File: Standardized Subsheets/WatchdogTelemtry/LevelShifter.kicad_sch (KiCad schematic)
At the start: 1 part, among them U6 LSF0204QPWRQ1

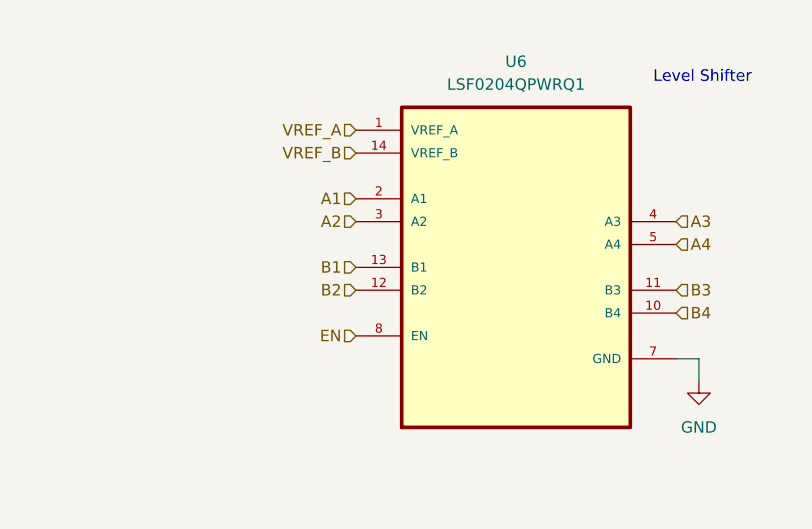
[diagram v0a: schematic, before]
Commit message: adding watchdog
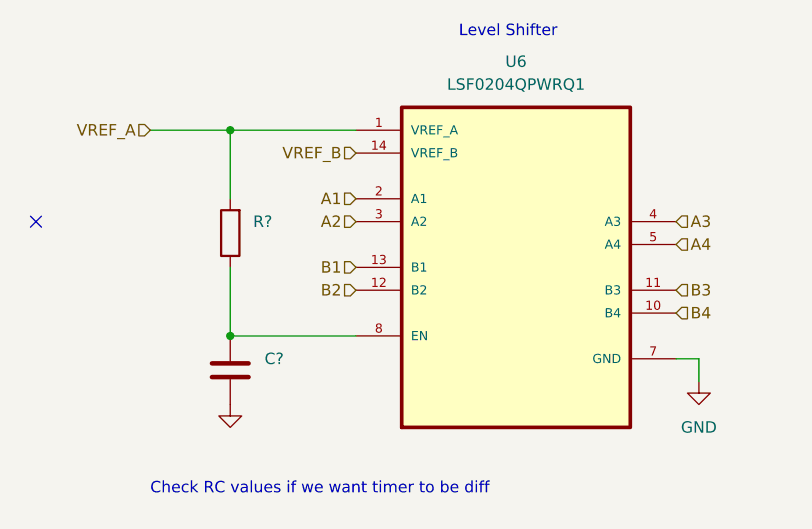
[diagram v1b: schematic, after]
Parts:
- added C?: (no value), symbol Device:C
- added R?: (no value), symbol Device:R
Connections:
- net GND: now also C?.2
- net VREF_A: now also R?.2
- net EN: no longer names the net of U6.8 (EN)
- net EN: now also C?.1, R?.1
- no-connect marks 0 -> 1
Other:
- note added: "Check RC values if we want timer to be diff"
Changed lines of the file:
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@@
 (kicad_sch (version 20211123) (generator eeschema)
   (paper "A4")
+  (junction (at 50.8 82.55) (diameter 0) (color 0 0 0 0)
+  )
+  (junction (at 50.8 59.69) (diameter 0) (color 0 0 0 0)
+  )
+  (no_connect (at 29.21 69.85))
+  (wire (pts (xy 50.8 59.69) (xy 50.8 67.31))
+    (stroke (width 0) (type default) (color 0 0 0 0))
+  )
+  (wire (pts (xy 41.91 59.69) (xy 50.8 59.69))
+    (stroke (width 0) (type default) (color 0 0 0 0))
+  )
+  (wire (pts (xy 50.8 59.69) (xy 64.77 59.69))
+    (stroke (width 0) (type default) (color 0 0 0 0))
+  )
+  (wire (pts (xy 50.8 74.93) (xy 50.8 82.55))
+    (stroke (width 0) (type default) (color 0 0 0 0))
+  )
+  (wire (pts (xy 50.8 82.55) (xy 64.77 82.55))
+    (stroke (width 0) (type default) (color 0 0 0 0))
+  )
   (wire (pts (xy 102.87 87.63) (xy 102.87 85.09))
     (stroke (width 0) (type default) (color 0 0 0 0))
@@
     (stroke (width 0) (type default) (color 0 0 0 0))
   )
-  (text "Level Shifter\n" (at 97.79 54.61 0)
+  (text "Check RC values if we want timer to be diff\n" (at 41.91 100.33 0)
     (effects (font (size 1.27 1.27)) (justify left bottom))
   )
-  (hierarchical_label "EN" (shape input) (at 64.77 82.55 180)
-    (effects (font (size 1.27 1.27)) (justify right))
+  (text "Level Shifter\n" (at 76.2 49.53 0)
+    (effects (font (size 1.27 1.27)) (justify left bottom))
   )
   (hierarchical_label "A3" (shape input) (at 100.33 69.85 0)
@@
     (effects (font (size 1.27 1.27)) (justify left))
   )
-  (hierarchical_label "VREF_A" (shape input) (at 64.77 59.69 180)
+  (hierarchical_label "VREF_A" (shape input) (at 41.91 59.69 180)
     (effects (font (size 1.27 1.27)) (justify right))
   )
   (hierarchical_label "A4" (shape input) (at 100.33 72.39 0)
     (effects (font (size 1.27 1.27)) (justify left))
+  )
+  (symbol (lib_id "Device:R") (at 50.8 71.12 180) (unit 1)
+    (in_bom yes) (on_board yes) (fields_autoplaced)
+    (property "Reference" "R?" (id 0) (at 53.34 69.8499 0)
+      (effects (font (size 1.27 1.27)) (justify right))
+    )
+    (property "Value" "" (id 1) (at 53.34 72.3899 0)
+      (effects (font (size 1.27 1.27)) (justify right))
+    )
+    (property "Footprint" "" (id 2) (at 52.578 71.12 90)
+      (effects (font (size 1.27 1.27)) hide)
+    )
+    (property "Datasheet" "~" (id 3) (at 50.8 71.12 0)
+      (effects (font (size 1.27 1.27)) hide)
+    )
+    (pin "1")
+    (pin "2")
+  )
+  (symbol (lib_id "Device:C") (at 50.8 86.36 0) (unit 1)
+    (in_bom yes) (on_board yes) (fields_autoplaced)
+    (property "Reference" "C?" (id 0) (at 54.61 85.0899 0)
+      (effects (font (size 1.27 1.27)) (justify left))
+    )
+    (property "Value" "" (id 1) (at 54.61 87.6299 0)
+      (effects (font (size 1.27 1.27)) (justify left))
+    )
+    (property "Footprint" "" (id 2) (at 51.7652 90.17 0)
+      (effects (font (size 1.27 1.27)) hide)
+    )
+    (property "Datasheet" "~" (id 3) (at 50.8 86.36 0)
+      (effects (font (size 1.27 1.27)) hide)
+    )
+    (pin "1")
+    (pin "2")
+  )
+  (symbol (lib_id "power:GND") (at 50.8 90.17 0) (unit 1)
+    (in_bom yes) (on_board yes) (fields_autoplaced)
+    (property "Reference" "#PWR?" (id 0) (at 50.8 96.52 0)
+      (effects (font (size 1.27 1.27)) hide)
+    )
+    (property "Value" "" (id 1) (at 50.8 95.25 0))
+    (property "Footprint" "" (id 2) (at 50.8 90.17 0)
+      (effects (font (size 1.27 1.27)) hide)
+    )
+    (property "Datasheet" "" (id 3) (at 50.8 90.17 0)
+      (effects (font (size 1.27 1.27)) hide)
+    )
+    (pin "1")
   )
   (symbol (lib_id "LSF0204QPWRQ1:LSF0204QPWRQ1") (at 82.55 74.93 0) (unit 1)
@@
       (effects (font (size 1.27 1.27)) (justify left bottom) hide)
     )
-    (property "Datasheet" "" (id 3) (at 82.55 74.93 0)
+    (property "Datasheet" "https://www.ti.com/lit/ds/symlink/lsf0204-q1.pdf?ts=1668512599421&ref_url=https%253A%252F%252Fwww.ti.com%252Fproduct%252FLSF0204-Q1%252Fpart-details%252FLSF0204QPWRQ1%253Futm_source%253Dgoogle%2526utm_medium%253Dcpc%2526utm_campaign%253Docb-tistore-promo-asc_opn_en-cpc-storeic-google-wwe%2526utm_content%253DDevice%2526ds_k%253DLSF0204QPWRQ1%2526DCM%253Dyes%2526gclid%253DCjwKCAiAjs2bBhACEiwALTBWZYsrvH2Lh7WvnQkqr_CpO-UcqyUhsEQ4HDqsQeB2dCVQx2F2--Vr3xoCQNgQAvD_BwE%2526gclsrc%253Daw.ds" (id 3) (at 82.55 74.93 0)
       (effects (font (size 1.27 1.27)) (justify left bottom) hide)
     )

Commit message: updated ADC and LS
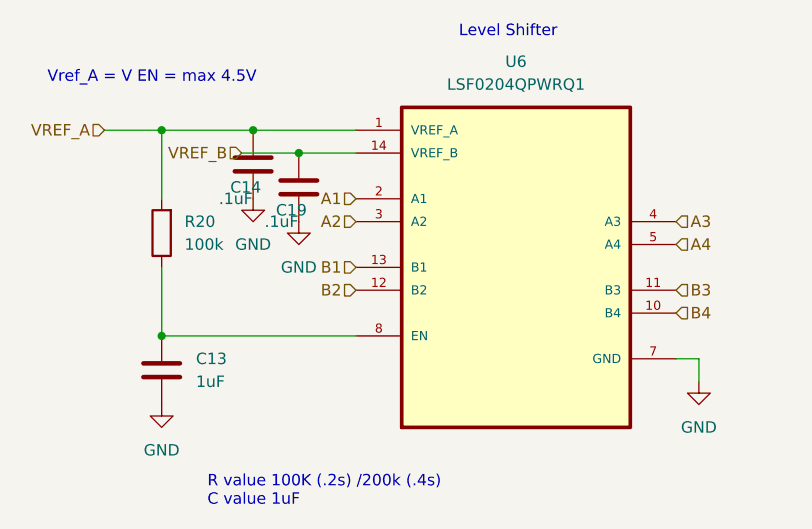
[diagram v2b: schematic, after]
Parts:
- added C14, C19: .1uF, Capacitor_SMD:C_0603_1608Metric, symbol Device:C
- C13: renamed from C?; value (none) -> 1uF; footprint (none) -> Capacitor_SMD:C_0603_1608Metric
- R20: renamed from R?; value (none) -> 100k; footprint (none) -> Resistor_SMD:R_0603_1608Metric
- U6: footprint SOP65P640X120-14N -> Package_SO:TSSOP-14_4.4x5mm_P0.65mm
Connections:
- net GND: now also C14.2, C19.2
- net VREF_A: now also C14.1
- net VREF_B: now also C19.1
- no-connect marks 1 -> 0
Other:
- note added: "R value 100K (.2s) /200k (.4s) C value 1uF"
- note added: "Vref_A = V EN = max 4.5V"
- note removed: "Check RC values if we want timer to be diff"
- moved on the sheet: C13, R20
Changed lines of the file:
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@@
 (kicad_sch (version 20211123) (generator eeschema)
   (paper "A4")
-  (junction (at 50.8 82.55) (diameter 0) (color 0 0 0 0)
-  )
-  (junction (at 50.8 59.69) (diameter 0) (color 0 0 0 0)
-  )
-  (no_connect (at 29.21 69.85))
-  (wire (pts (xy 50.8 59.69) (xy 50.8 67.31))
-    (stroke (width 0) (type default) (color 0 0 0 0))
-  )
-  (wire (pts (xy 41.91 59.69) (xy 50.8 59.69))
-    (stroke (width 0) (type default) (color 0 0 0 0))
-  )
-  (wire (pts (xy 50.8 59.69) (xy 64.77 59.69))
-    (stroke (width 0) (type default) (color 0 0 0 0))
-  )
-  (wire (pts (xy 50.8 74.93) (xy 50.8 82.55))
-    (stroke (width 0) (type default) (color 0 0 0 0))
-  )
-  (wire (pts (xy 50.8 82.55) (xy 64.77 82.55))
+  (junction (at 58.42 62.23) (diameter 0) (color 0 0 0 0)
+  )
+  (junction (at 43.18 82.55) (diameter 0) (color 0 0 0 0)
+  )
+  (junction (at 43.18 59.69) (diameter 0) (color 0 0 0 0)
+  )
+  (junction (at 53.34 59.69) (diameter 0) (color 0 0 0 0)
+  )
+  (wire (pts (xy 43.18 59.69) (xy 43.18 67.31))
+    (stroke (width 0) (type default) (color 0 0 0 0))
+  )
+  (wire (pts (xy 36.83 59.69) (xy 43.18 59.69))
+    (stroke (width 0) (type default) (color 0 0 0 0))
+  )
+  (wire (pts (xy 43.18 74.93) (xy 43.18 82.55))
+    (stroke (width 0) (type default) (color 0 0 0 0))
+  )
+  (wire (pts (xy 53.34 59.69) (xy 64.77 59.69))
+    (stroke (width 0) (type default) (color 0 0 0 0))
+  )
+  (wire (pts (xy 43.18 59.69) (xy 53.34 59.69))
+    (stroke (width 0) (type default) (color 0 0 0 0))
+  )
+  (wire (pts (xy 58.42 62.23) (xy 64.77 62.23))
+    (stroke (width 0) (type default) (color 0 0 0 0))
+  )
+  (wire (pts (xy 43.18 82.55) (xy 64.77 82.55))
+    (stroke (width 0) (type default) (color 0 0 0 0))
+  )
+  (wire (pts (xy 52.07 62.23) (xy 58.42 62.23))
     (stroke (width 0) (type default) (color 0 0 0 0))
   )
@@
     (stroke (width 0) (type default) (color 0 0 0 0))
   )
-  (text "Check RC values if we want timer to be diff\n" (at 41.91 100.33 0)
+  (text "Vref_A = V EN = max 4.5V\n" (at 30.48 54.61 0)
+    (effects (font (size 1.27 1.27)) (justify left bottom))
+  )
+  (text "R value 100K (.2s) /200k (.4s)\nC value 1uF\n" (at 48.26 101.6 0)
     (effects (font (size 1.27 1.27)) (justify left bottom))
   )
@@
     (effects (font (size 1.27 1.27)) (justify left))
   )
-  (hierarchical_label "VREF_B" (shape input) (at 64.77 62.23 180)
+  (hierarchical_label "VREF_B" (shape input) (at 52.07 62.23 180)
     (effects (font (size 1.27 1.27)) (justify right))
   )
@@
     (effects (font (size 1.27 1.27)) (justify left))
   )
-  (hierarchical_label "VREF_A" (shape input) (at 41.91 59.69 180)
+  (hierarchical_label "VREF_A" (shape input) (at 36.83 59.69 180)
     (effects (font (size 1.27 1.27)) (justify right))
   )
@@
     (effects (font (size 1.27 1.27)) (justify left))
   )
-  (symbol (lib_id "Device:R") (at 50.8 71.12 180) (unit 1)
-    (in_bom yes) (on_board yes) (fields_autoplaced)
-    (property "Reference" "R?" (id 0) (at 53.34 69.8499 0)
+  (symbol (lib_id "Device:R") (at 43.18 71.12 180) (unit 1)
+    (in_bom yes) (on_board yes) (fields_autoplaced)
+    (property "Reference" "R20" (id 0) (at 45.72 69.8499 0)
       (effects (font (size 1.27 1.27)) (justify right))
     )
-    (property "Value" "" (id 1) (at 53.34 72.3899 0)
+    (property "Value" "100k" (id 1) (at 45.72 72.3899 0)
       (effects (font (size 1.27 1.27)) (justify right))
     )
-    (property "Footprint" "" (id 2) (at 52.578 71.12 90)
-      (effects (font (size 1.27 1.27)) hide)
-    )
-    (property "Datasheet" "~" (id 3) (at 50.8 71.12 0)
-      (effects (font (size 1.27 1.27)) hide)
-    )
-    (pin "1")
-    (pin "2")
-  )
-  (symbol (lib_id "Device:C") (at 50.8 86.36 0) (unit 1)
-    (in_bom yes) (on_board yes) (fields_autoplaced)
-    (property "Reference" "C?" (id 0) (at 54.61 85.0899 0)
-      (effects (font (size 1.27 1.27)) (justify left))
-    )
-    (property "Value" "" (id 1) (at 54.61 87.6299 0)
-      (effects (font (size 1.27 1.27)) (justify left))
-    )
-    (property "Footprint" "" (id 2) (at 51.7652 90.17 0)
-      (effects (font (size 1.27 1.27)) hide)
-    )
-    (property "Datasheet" "~" (id 3) (at 50.8 86.36 0)
-      (effects (font (size 1.27 1.27)) hide)
-    )
-    (pin "1")
-    (pin "2")
-  )
-  (symbol (lib_id "power:GND") (at 50.8 90.17 0) (unit 1)
-    (in_bom yes) (on_board yes) (fields_autoplaced)
-    (property "Reference" "#PWR?" (id 0) (at 50.8 96.52 0)
-      (effects (font (size 1.27 1.27)) hide)
-    )
-    (property "Value" "" (id 1) (at 50.8 95.25 0))
-    (property "Footprint" "" (id 2) (at 50.8 90.17 0)
-      (effects (font (size 1.27 1.27)) hide)
-    )
-    (property "Datasheet" "" (id 3) (at 50.8 90.17 0)
-      (effects (font (size 1.27 1.27)) hide)
-    )
-    (pin "1")
+    (property "Footprint" "Resistor_SMD:R_0603_1608Metric" (id 2) (at 44.958 71.12 90)
+      (effects (font (size 1.27 1.27)) hide)
+    )
+    (property "Datasheet" "~" (id 3) (at 43.18 71.12 0)
+      (effects (font (size 1.27 1.27)) hide)
+    )
+    (pin "1")
+    (pin "2")
+  )
+  (symbol (lib_id "Device:C") (at 53.34 63.5 0) (unit 1)
+    (in_bom yes) (on_board yes)
+    (property "Reference" "C14" (id 0) (at 50.8 66.04 0)
+      (effects (font (size 1.27 1.27)) (justify left))
+    )
+    (property "Value" ".1uF" (id 1) (at 49.53 67.31 0)
+      (effects (font (size 1.27 1.27)) (justify left))
+    )
+    (property "Footprint" "Capacitor_SMD:C_0603_1608Metric" (id 2) (at 54.3052 67.31 0)
+      (effects (font (size 1.27 1.27)) hide)
+    )
+    (property "Datasheet" "~" (id 3) (at 53.34 63.5 0)
+      (effects (font (size 1.27 1.27)) hide)
+    )
+    (pin "1")
+    (pin "2")
+  )
+  (symbol (lib_id "Device:C") (at 43.18 86.36 0) (unit 1)
+    (in_bom yes) (on_board yes) (fields_autoplaced)
+    (property "Reference" "C13" (id 0) (at 46.99 85.0899 0)
+      (effects (font (size 1.27 1.27)) (justify left))
+    )
+    (property "Value" "1uF" (id 1) (at 46.99 87.6299 0)
+      (effects (font (size 1.27 1.27)) (justify left))
+    )
+    (property "Footprint" "Capacitor_SMD:C_0603_1608Metric" (id 2) (at 44.1452 90.17 0)
+      (effects (font (size 1.27 1.27)) hide)
+    )
+    (property "Datasheet" "~" (id 3) (at 43.18 86.36 0)
+      (effects (font (size 1.27 1.27)) hide)
+    )
+    (pin "1")
+    (pin "2")
+  )
+  (symbol (lib_id "power:GND") (at 43.18 90.17 0) (unit 1)
+    (in_bom yes) (on_board yes) (fields_autoplaced)
+    (property "Reference" "#PWR0104" (id 0) (at 43.18 96.52 0)
+      (effects (font (size 1.27 1.27)) hide)
+    )
+    (property "Value" "GND" (id 1) (at 43.18 95.25 0))
+    (property "Footprint" "" (id 2) (at 43.18 90.17 0)
+      (effects (font (size 1.27 1.27)) hide)
+    )
+    (property "Datasheet" "" (id 3) (at 43.18 90.17 0)
+      (effects (font (size 1.27 1.27)) hide)
+    )
+    (pin "1")
+  )
+  (symbol (lib_id "Device:C") (at 58.42 66.04 0) (unit 1)
+    (in_bom yes) (on_board yes)
+    (property "Reference" "C19" (id 0) (at 55.88 68.58 0)
+      (effects (font (size 1.27 1.27)) (justify left))
+    )
+    (property "Value" ".1uF" (id 1) (at 54.61 69.85 0)
+      (effects (font (size 1.27 1.27)) (justify left))
+    )
+    (property "Footprint" "Capacitor_SMD:C_0603_1608Metric" (id 2) (at 59.3852 69.85 0)
+      (effects (font (size 1.27 1.27)) hide)
+    )
+    (property "Datasheet" "~" (id 3) (at 58.42 66.04 0)
+      (effects (font (size 1.27 1.27)) hide)
+    )
+    (pin "1")
+    (pin "2")
   )
   (symbol (lib_id "LSF0204QPWRQ1:LSF0204QPWRQ1") (at 82.55 74.93 0) (unit 1)
@@
     (property "Reference" "U6" (id 0) (at 82.55 52.07 0))
     (property "Value" "LSF0204QPWRQ1" (id 1) (at 82.55 54.61 0))
-    (property "Footprint" "SOP65P640X120-14N" (id 2) (at 82.55 74.93 0)
+    (property "Footprint" "Package_SO:TSSOP-14_4.4x5mm_P0.65mm" (id 2) (at 82.55 74.93 0)
       (effects (font (size 1.27 1.27)) (justify left bottom) hide)
     )
@@
       (effects (font (size 1.27 1.27)) hide)
     )
+    (pin "1")
+  )
+  (symbol (lib_id "power:GND") (at 53.34 67.31 0) (unit 1)
+    (in_bom yes) (on_board yes) (fields_autoplaced)
+    (property "Reference" "#PWR0101" (id 0) (at 53.34 73.66 0)
+      (effects (font (size 1.27 1.27)) hide)
+    )
+    (property "Value" "GND" (id 1) (at 53.34 72.39 0))
+    (property "Footprint" "" (id 2) (at 53.34 67.31 0)
+      (effects (font (size 1.27 1.27)) hide)
+    )
+    (property "Datasheet" "" (id 3) (at 53.34 67.31 0)
+      (effects (font (size 1.27 1.27)) hide)
+    )
+    (pin "1")
+  )
+  (symbol (lib_id "power:GND") (at 58.42 69.85 0) (unit 1)
+    (in_bom yes) (on_board yes) (fields_autoplaced)
+    (property "Reference" "#PWR0103" (id 0) (at 58.42 76.2 0)
+      (effects (font (size 1.27 1.27)) hide)
+    )
+    (property "Value" "GND" (id 1) (at 58.42 74.93 0))
+    (property "Footprint" "" (id 2) (at 58.42 69.85 0)
+      (effects (font (size 1.27 1.27)) hide)
+    )
+    (property "Datasheet" "" (id 3) (at 58.42 69.85 0)
+      (effects (font (size 1.27 1.27)) hide)
+    )
